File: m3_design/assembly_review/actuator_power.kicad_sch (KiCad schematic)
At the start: 14 parts, among them Q120 AON6403, Q121 AON6403, Q122 AO3400A

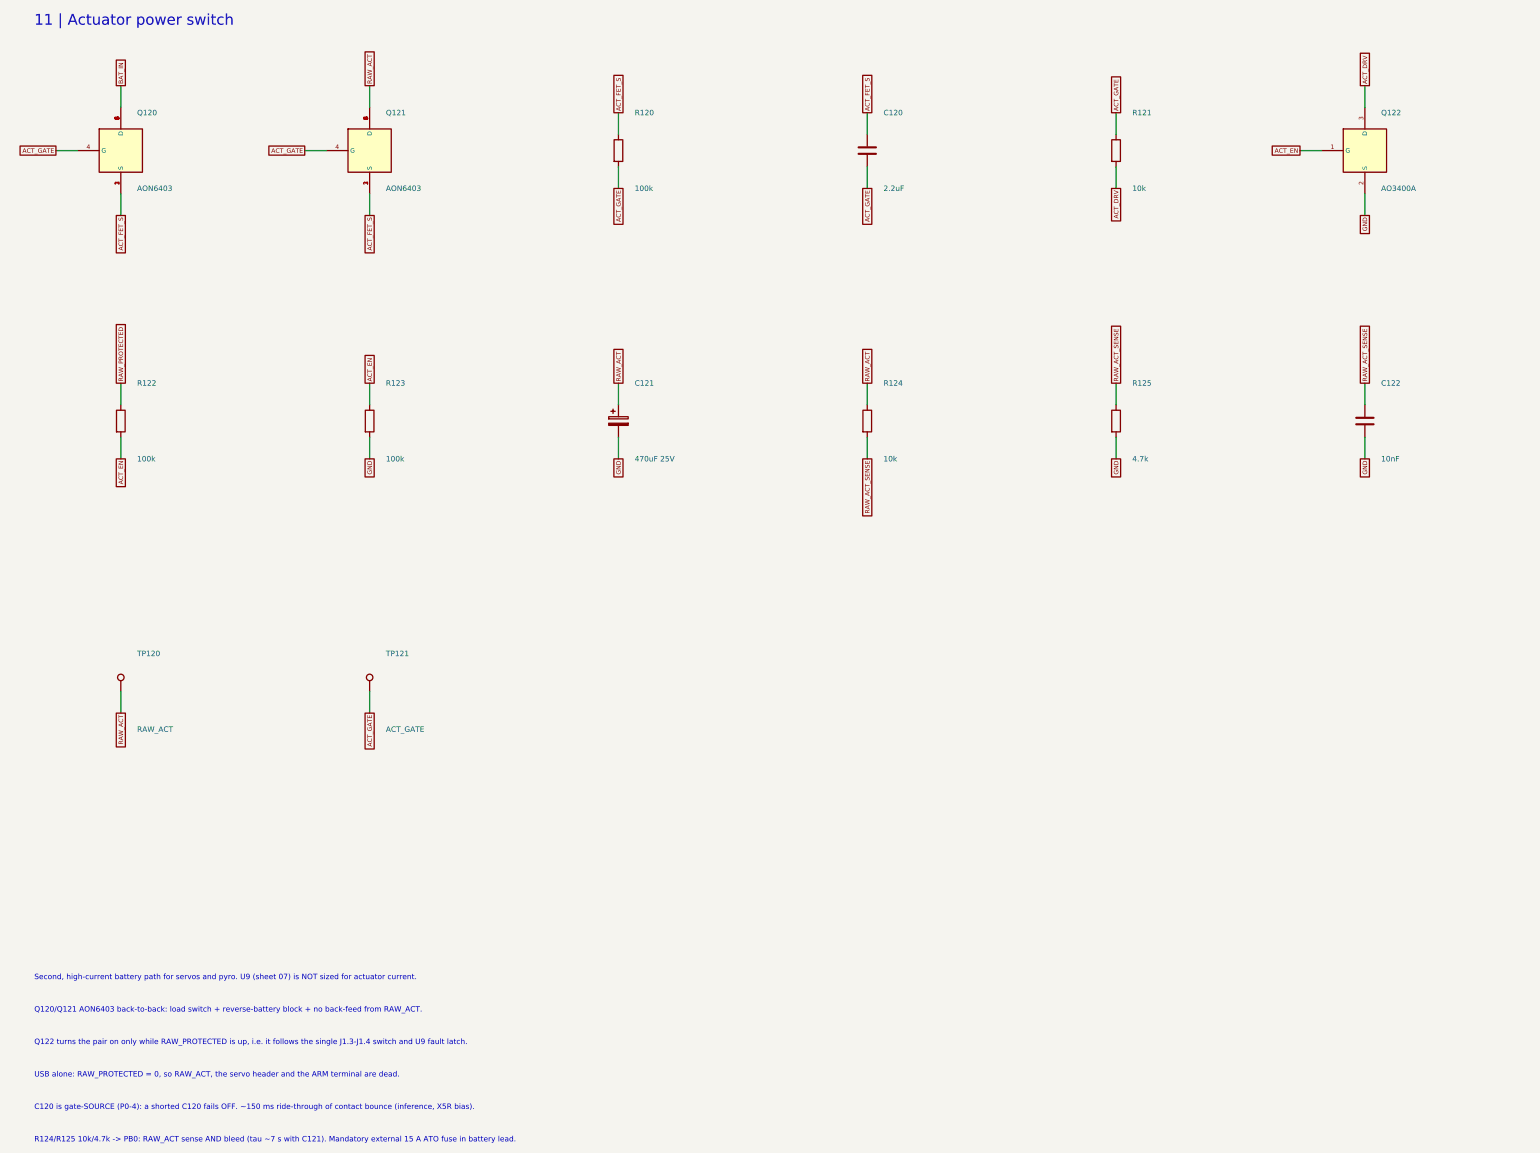
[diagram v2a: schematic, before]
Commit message: M3-ASSY-R4: R3 validation fixes, new IMU, fault-tolerant pyro sensing
The board, schematic sheets and footprint library are generated from
R3 (533af8e) by m3_design/r4_build.sh (r4_lib.py, r4_sch.py,
r4_pcb.py). docs/REQUIREMENTS.md states what the board must do;
docs/M3_R4.md records every change, the thirteen evaluation passes
(twelve independent reviews) and the accepted deviations.

- IMU: ST LSM6DSV320X (16 g and 320 g, 4000 dps)
- Pyro: black ARM and orange igniter terminals, eight pyro spacing
  rules in m3.kicad_dru, sense dividers of 2 x 5.1k over 2 x 2k in
  parallel, 4.7k at each ADC pin (R168-R172)
- Pull-pin on a JST PH connector; JLC tooling holes
- Fab: Standard PCBA, 84 BOM lines, 205 placed parts, $80.12 per board
  at five boards (tools/jlc_cost.py); placement rotations verified
- Gate: tools/check.sh DRC 0, unconnected 0, schematic parity 0, ERC 0,
  audit OK; m3_design/check_actuators.py OK

Nothing has been built or measured, and there is no R4 firmware. The
open owner decisions and the bench tests are listed in STATUS.md.

Co-Authored-By: Claude Opus 5.5 <noreply@anthropic.com>
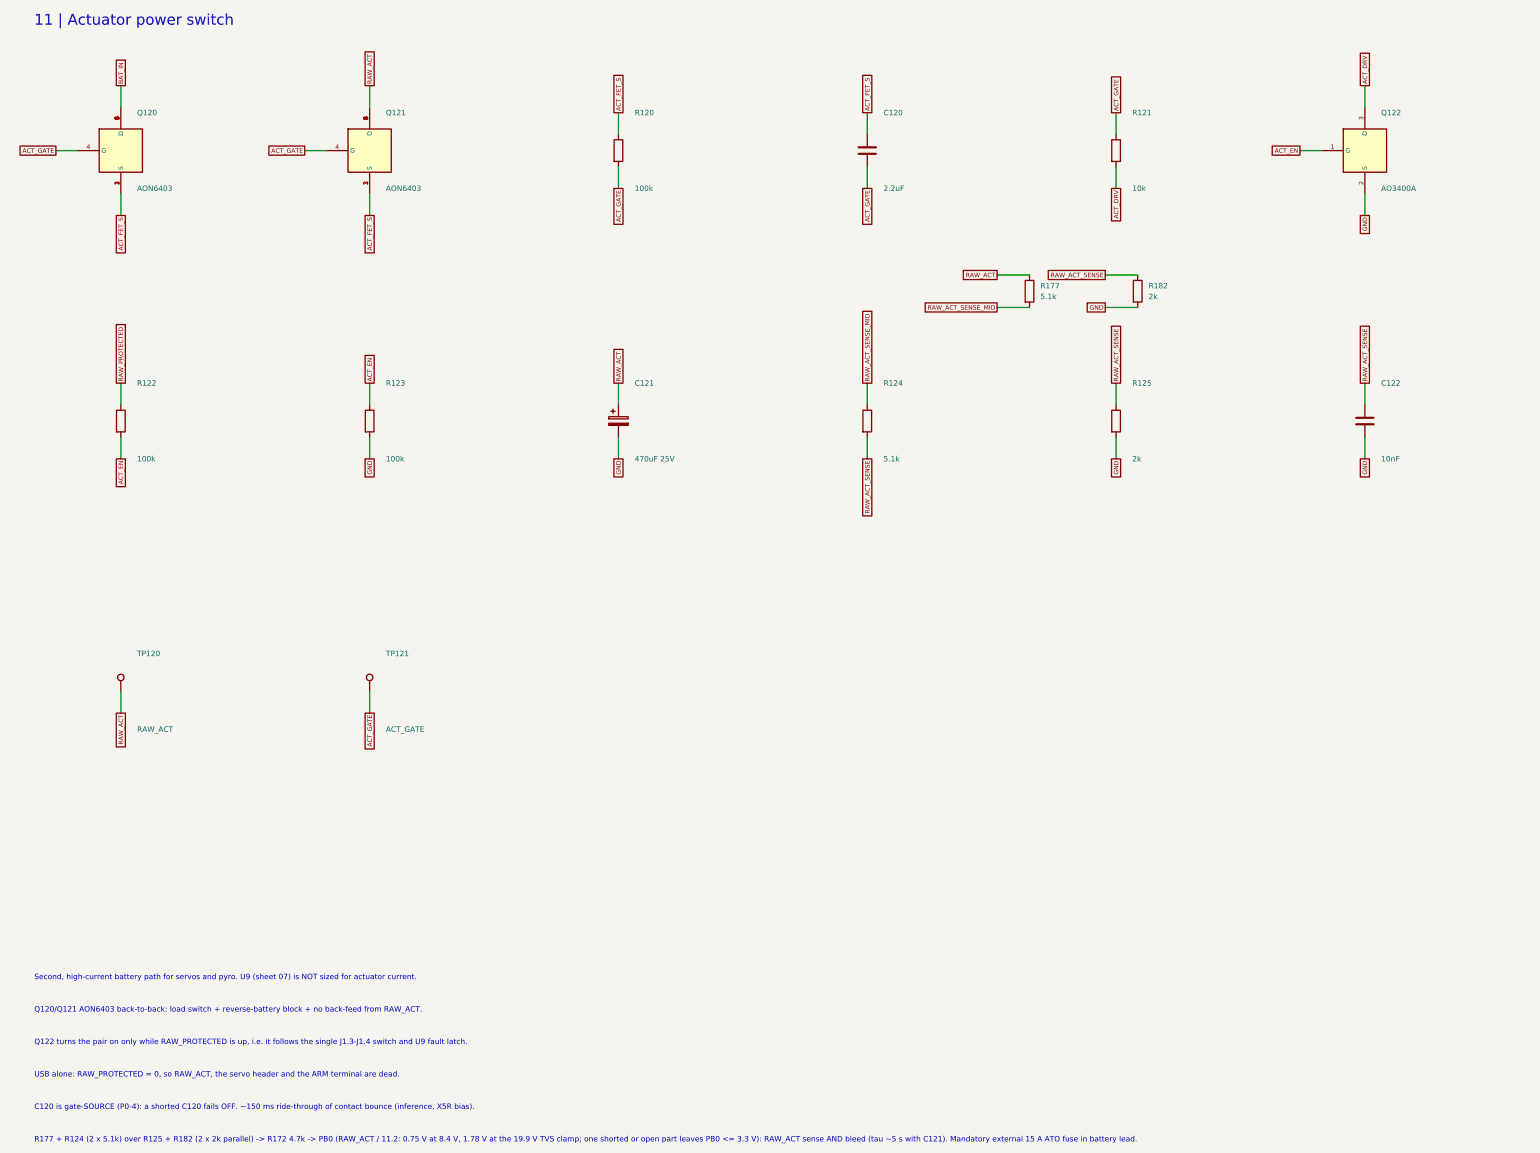
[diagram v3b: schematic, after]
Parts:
- added R177: 5.1k, rocket:R0402, symbol M3:R
- added R182: 2k, rocket:R0402, symbol M3:R
- R124: value 10k -> 5.1k; LCSC C25744 -> C25905
- R125: value 4.7k -> 2k; LCSC C25900 -> C4109
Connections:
- net GND: now also R182.2
- net RAW_ACT: now also R177.1; no longer R124.1
- net RAW_ACT_SENSE: now also R182.1
- new net RAW_ACT_SENSE_MID: R124.1, R177.2
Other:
- note added: "R177 + R124 (2 x 5.1k) over R125 + R182 (2 x 2k parallel) -> R172 4.7k -> PB0 (RAW_ACT / 11.2: 0.75 V at 8.4 V, 1.78 V at the 19.9 V TVS clamp; one shorted or open part leaves PB0 <= 3.3 V): RAW_ACT sense AND bleed (tau ~5 s with C121). Mandatory external 15 A ATO fuse in battery lead."
- note removed: "R124/R125 10k/4.7k -> PB0: RAW_ACT sense AND bleed (tau ~7 s with C121). Mandatory external 15 A ATO fuse in battery lead."
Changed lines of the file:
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@@
 		(title "11 | Actuator power switch")
 		(date "2026-09-25")
-		(rev "M3-ASSY-R3")
+		(rev "M3-ASSY-R4")
 		(company "Single-board M3 candidate; actuator merge, not bench-verified"))
 	(symbol
@@
 					(size 1.27 1.27))
 				(justify left)))
-		(property "Value" "10k"
+		(property "Value" "5.1k"
 			(at 219.71 123.19 0)
 			(effects
@@
 				(font
 					(size 1.27 1.27))))
-		(property "LCSC" "C25744"
+		(property "LCSC" "C25905"
 			(at 215.9 114.3 0)
 			(hide yes)
@@
 			(type default))
 )
-	(global_label "RAW_ACT"
+	(global_label "RAW_ACT_SENSE_MID"
 		(shape passive)
 		(at 215.9 105.41 90)
@@
 					(size 1.27 1.27))
 				(justify left)))
-		(property "Value" "4.7k"
+		(property "Value" "2k"
 			(at 278.13 123.19 0)
 			(effects
@@
 				(font
 					(size 1.27 1.27))))
-		(property "LCSC" "C25900"
+		(property "LCSC" "C4109"
 			(at 274.32 114.3 0)
 			(hide yes)
@@
 			(justify left))
 )
-	(text "R124/R125 10k/4.7k -> PB0: RAW_ACT sense AND bleed (tau ~7 s with C121). Mandatory external 15 A ATO fuse in battery lead."
+	(text "R177 + R124 (2 x 5.1k) over R125 + R182 (2 x 2k parallel) -> R172 4.7k -> PB0 (RAW_ACT / 11.2: 0.75 V at 8.4 V, 1.78 V at the 19.9 V TVS clamp; one shorted or open part leaves PB0 <= 3.3 V): RAW_ACT sense AND bleed (tau ~5 s with C121). Mandatory external 15 A ATO fuse in battery lead."
 		(at 20.32 283.1 0)
 		(effects
@@
 			(justify left))
 )
+	(symbol
+		(lib_id "M3:R")
+		(at 254 83.82 0)
+		(unit 1)
+		(in_bom yes)
+		(on_board yes)
+		(dnp no)
+		(property "Reference" "R177"
+			(at 256.54 82.55 0)
+			(effects
+				(font
+					(size 1.27 1.27))
+				(justify left)))
+		(property "Value" "5.1k"
+			(at 256.54 85.09 0)
+			(effects
+				(font
+					(size 1.27 1.27))
+				(justify left)))
+		(property "Footprint" "rocket:R0402"
+			(at 254 83.82 0)
+			(hide yes)
+			(effects
+				(font
+					(size 1.27 1.27))
+				(justify left)))
+		(property "Datasheet" ""
+			(at 254 83.82 0)
+			(hide yes)
+			(effects
+				(font
+					(size 1.27 1.27))
+				(justify left)))
+		(property "LCSC" "C25905"
+			(at 254 83.82 0)
+			(hide yes)
+			(effects
+				(font
+					(size 1.27 1.27))
+				(justify left)))
+		(instances
+			(project "m3"
+				(path "/6007a7db-6a58-5660-8beb-956dea045ff8/6133d301-6422-5dca-9dda-573ff465fb31"
+					(reference "R177")
+					(unit 1)))))
+	(wire
+		(pts
+			(xy 254 80.01)
+			(xy 246.38 80.01))
+		(stroke
+			(width 0)
+			(type default))
+)
+	(global_label "RAW_ACT"
+		(shape passive)
+		(at 246.38 80.01 0)
+		(effects
+			(font
+				(size 1.05 1.05))
+			(justify right))
+)
+	(wire
+		(pts
+			(xy 254 87.63)
+			(xy 246.38 87.63))
+		(stroke
+			(width 0)
+			(type default))
+)
+	(global_label "RAW_ACT_SENSE_MID"
+		(shape passive)
+		(at 246.38 87.63 0)
+		(effects
+			(font
+				(size 1.05 1.05))
+			(justify right))
+)
+	(symbol
+		(lib_id "M3:R")
+		(at 279.4 83.82 0)
+		(unit 1)
+		(in_bom yes)
+		(on_board yes)
+		(dnp no)
+		(property "Reference" "R182"
+			(at 281.94 82.55 0)
+			(effects
+				(font
+					(size 1.27 1.27))
+				(justify left)))
+		(property "Value" "2k"
+			(at 281.94 85.09 0)
+			(effects
+				(font
+					(size 1.27 1.27))
+				(justify left)))
+		(property "Footprint" "rocket:R0402"
+			(at 279.4 83.82 0)
+			(hide yes)
+			(effects
+				(font
+					(size 1.27 1.27))
+				(justify left)))
+		(property "Datasheet" ""
+			(at 279.4 83.82 0)
+			(hide yes)
+			(effects
+				(font
+					(size 1.27 1.27))
+				(justify left)))
+		(property "LCSC" "C4109"
+			(at 279.4 83.82 0)
+			(hide yes)
+			(effects
+				(font
+					(size 1.27 1.27))
+				(justify left)))
+		(instances
+			(project "m3"
+				(path "/6007a7db-6a58-5660-8beb-956dea045ff8/6133d301-6422-5dca-9dda-573ff465fb31"
+					(reference "R182")
+					(unit 1)))))
+	(wire
+		(pts
+			(xy 279.4 80.01)
+			(xy 271.78 80.01))
+		(stroke
+			(width 0)
+			(type default))
+)
+	(global_label "RAW_ACT_SENSE"
+		(shape passive)
+		(at 271.78 80.01 0)
+		(effects
+			(font
+				(size 1.05 1.05))
+			(justify right))
+)
+	(wire
+		(pts
+			(xy 279.4 87.63)
+			(xy 271.78 87.63))
+		(stroke
+			(width 0)
+			(type default))
+)
+	(global_label "GND"
+		(shape passive)
+		(at 271.78 87.63 0)
+		(effects
+			(font
+				(size 1.05 1.05))
+			(justify right))
+)
 	(sheet_instances
